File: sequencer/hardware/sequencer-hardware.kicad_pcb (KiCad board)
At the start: 4 copper layers, 98.4 x 147.3 mm, 136 parts, among them J1 Barrel Jack, J10 JST_4-pin_male, J11 Conn_01x03, J12 Conn_01x03, J13 Conn_01x03, J14 Conn_01x03, J15 JST_4-pin_male, J16 JST_4-pin_male, J17 Conn_01x03, J18 JST_4-pin_male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

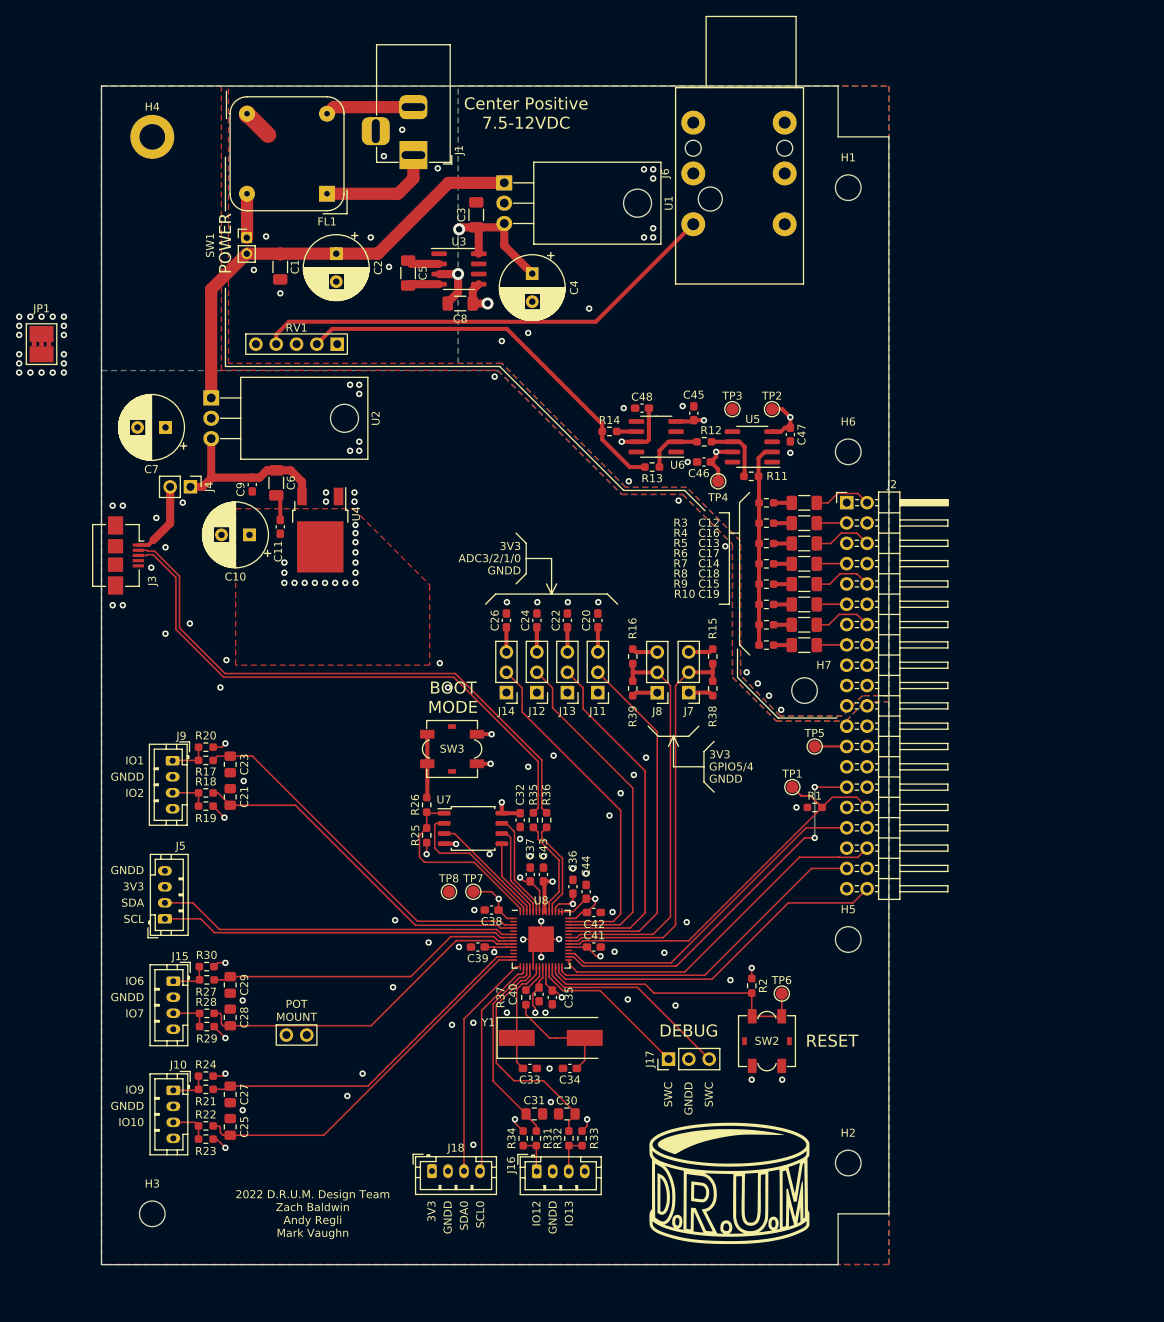
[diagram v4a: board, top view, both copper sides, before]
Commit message: move 40-pin connector
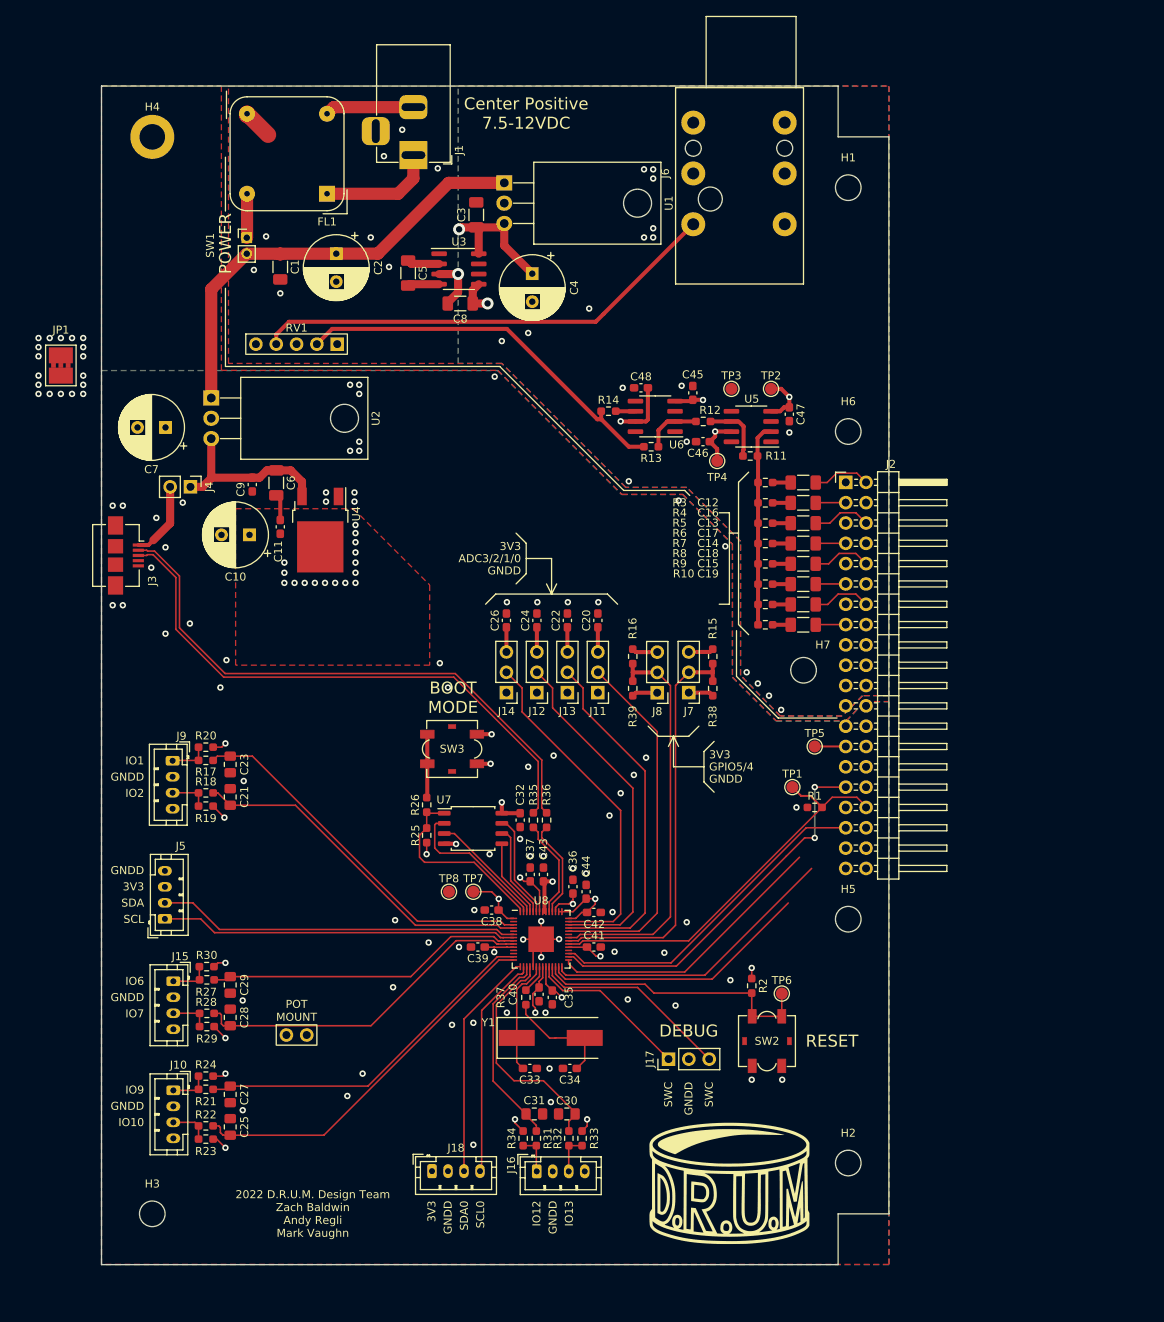
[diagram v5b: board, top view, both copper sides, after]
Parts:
- moved JP1 3.60 mm to (20.6, 60.3)
- moved C46 2.54 mm to (100.8, 69.8)
- moved C48 2.54 mm to (93.1, 63.1)
- moved R10 2.54 mm to (108.6, 92.7)
- moved R11 2.54 mm to (106.7, 71.6)
- moved R3 2.54 mm to (108.6, 75.0)
- moved R4 2.54 mm to (108.6, 77.5)
- moved R6 2.54 mm to (108.6, 82.6)
- moved R8 2.54 mm to (108.6, 87.7)
- moved C12 2.54 mm to (113.4, 75.0)
- moved C16 2.54 mm to (113.4, 77.5)
- moved C17 2.54 mm to (113.4, 82.6)
- moved C18 2.54 mm to (113.4, 87.7)
- moved C19 2.54 mm to (113.4, 92.7)
- moved H7 2.54 mm to (113.4, 98.4)
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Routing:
- net /CBUS_EXTRA: track 44.3 -> 33.7 mm
- net /CBUS_SCK: track 44.6 -> 35.7 mm
- net /CBUS_DRDY: track 41.9 -> 37.5 mm
- net Net-(R13-Pad2): track 50.1 -> 48.8 mm
- net -5V: track 56.0 -> 55.0 mm
- net Net-(R11-Pad2): track 8.13 -> 7.24 mm

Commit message: Implement star grounding
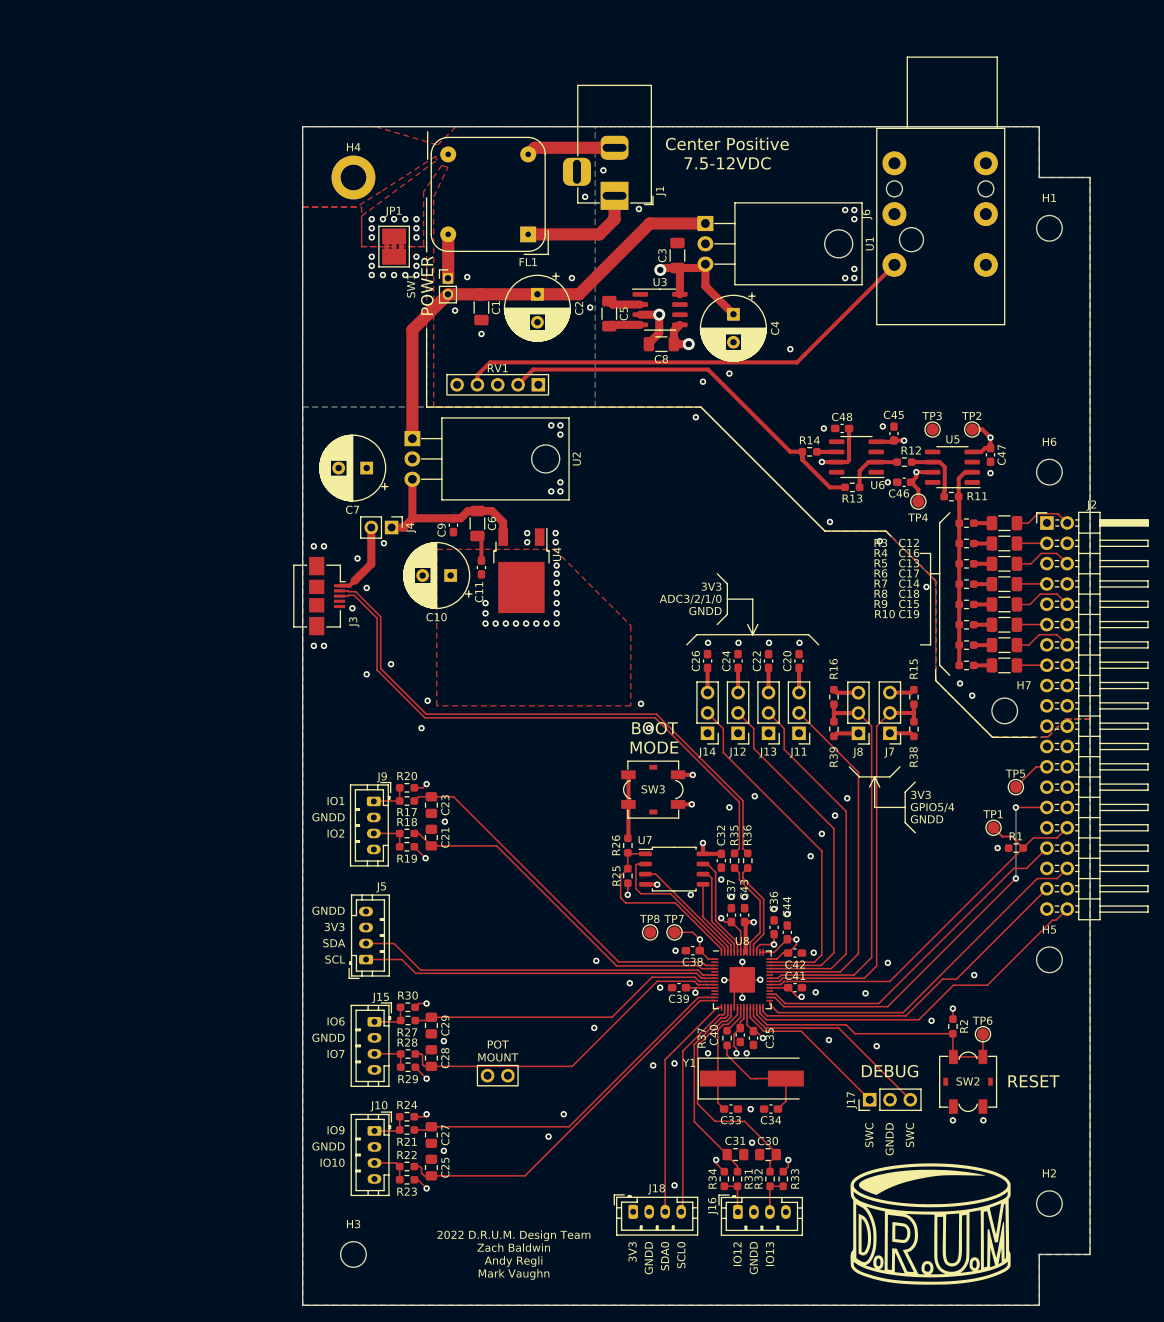
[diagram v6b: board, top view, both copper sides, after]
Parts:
- moved JP1 44.2 mm to (62.2, 45.5)
- moved H5 25.7 mm to (144.1, 134.6)
- moved SW2 25.7 mm to (134.0, 149.9)
- moved H1 25.7 mm to (144.1, 43.2)
- moved H2 25.7 mm to (144.1, 165.1)
- moved H6 25.7 mm to (144.1, 73.7)
- moved R2 25.7 mm to (132.1, 142.9)
- moved C23 25.7 mm to (66.9, 115.3)
- moved C25 25.7 mm to (66.9, 160.6)
- moved C28 25.7 mm to (66.9, 146.9)
- moved C10 25.7 mm to (69.3, 86.6)
- moved C21 25.7 mm to (66.9, 119.3)
- moved C27 25.7 mm to (66.9, 156.5)
- moved C29 25.7 mm to (66.9, 142.8)
- moved U2 25.7 mm to (64.5, 69.5)
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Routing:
- net /CBUS_EXTRA: track 33.7 -> 45.2 mm
- net /CBUS_SCK: track 35.7 -> 45.5 mm
- net /CBUS_DRDY: track 37.5 -> 42.8 mm
- net GNDA: track 10.5 -> 6.60 mm, vias 36 -> 34
- net /CBUS_SDRETIN: track 48.2 -> 50.6 mm
- net /CBUS_SDOUT: track 42.2 -> 43.2 mm
- net +5VD: track 26.1 -> 27.1 mm
- net Net-(R13-Pad2): track 48.8 -> 49.4 mm
- net GNDD: vias 86 -> 87
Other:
- outline, holes or cut-outs redrawn
